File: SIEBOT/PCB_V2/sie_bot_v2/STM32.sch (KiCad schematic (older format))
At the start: 27 parts, among them P8 CONN_12X2, P9 CONN_12X2, U10 STM32F105RC, U11 LT1117CST-3.3, X3 8MHz

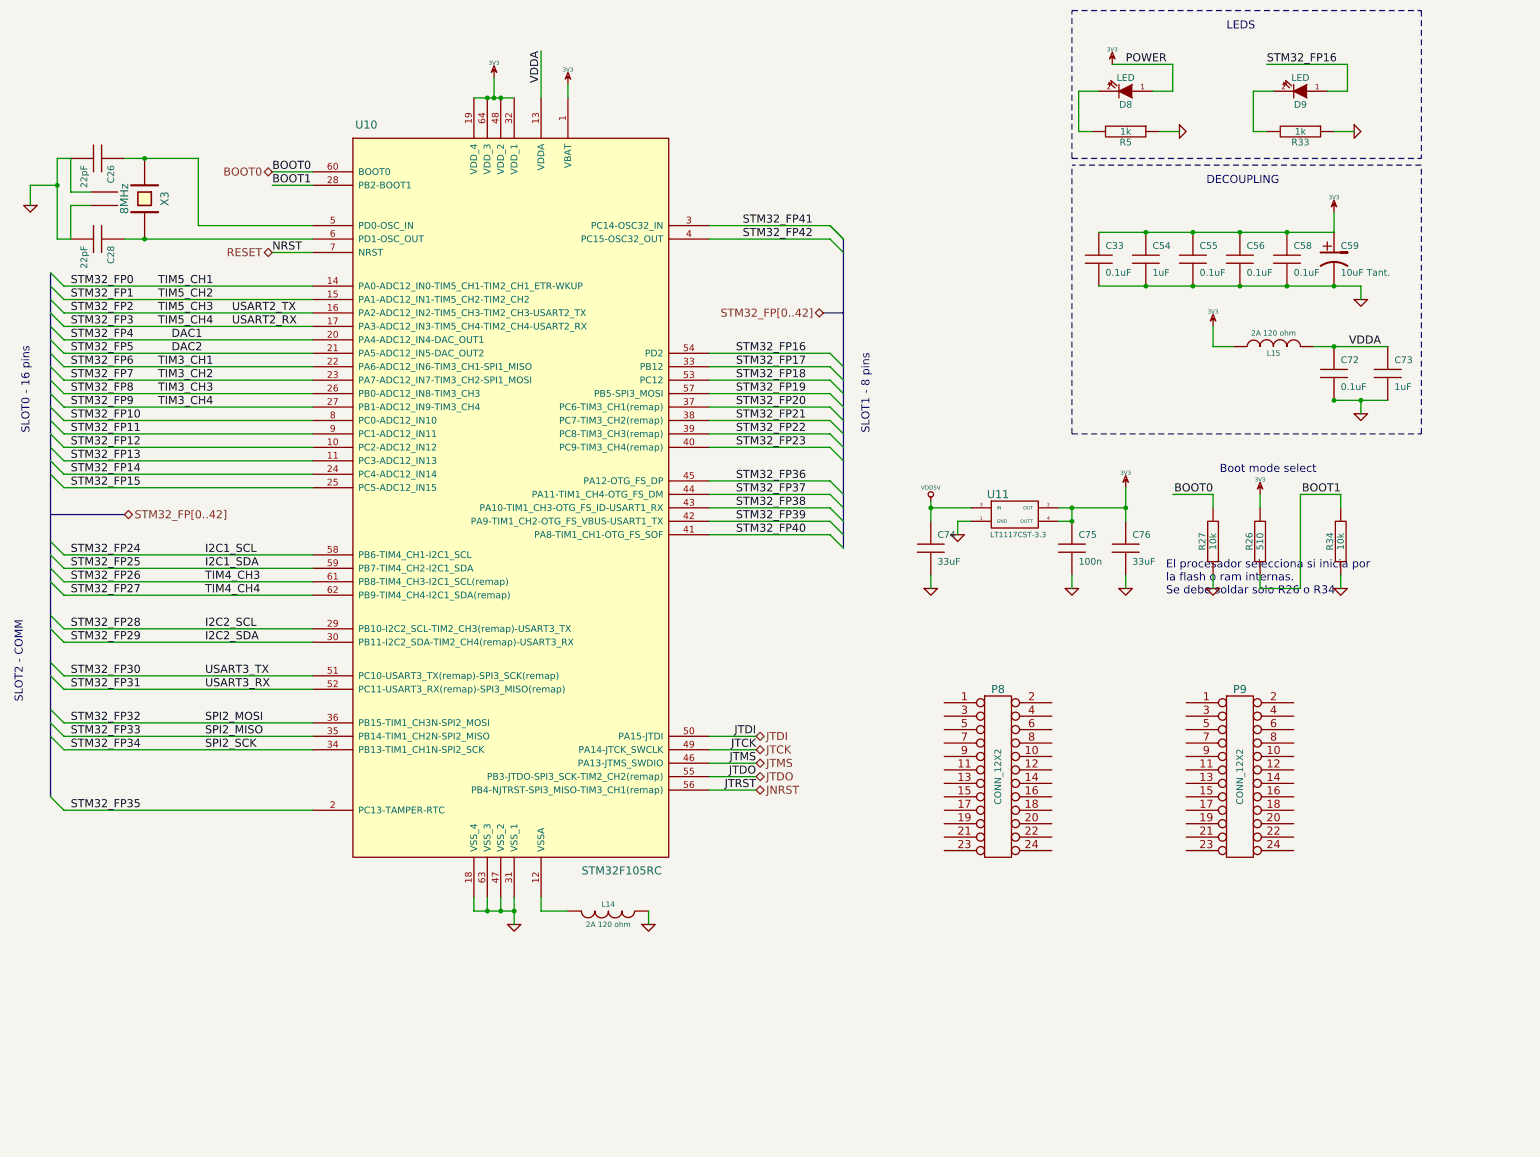
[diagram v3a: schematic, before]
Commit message: Coenxión y ruteo de los GPIO del STM32 t los conectores
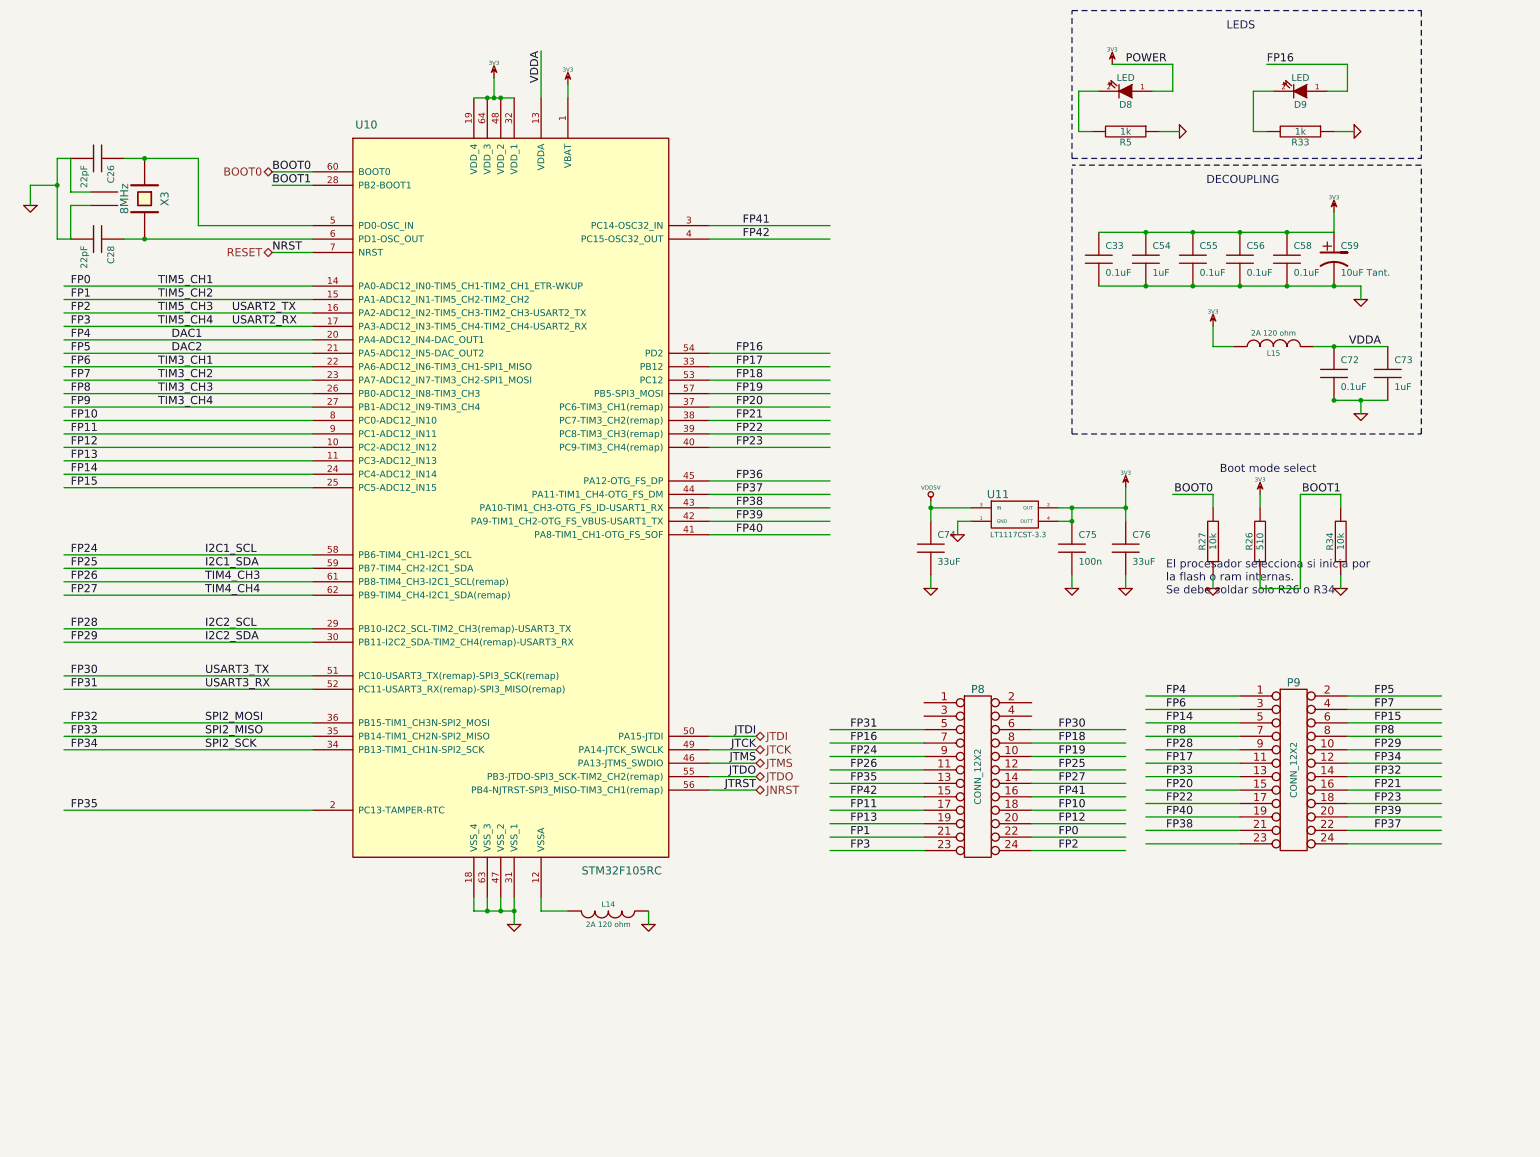
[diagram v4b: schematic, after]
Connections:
- net labels added: FP0, FP1, FP10, FP11, FP12, FP13, FP14, FP15, FP16, FP17, FP18, FP19, FP2, FP20, FP21, FP22, FP23, FP24, FP25, FP26, FP27, FP28, FP29, FP3, FP30, FP31, FP32, FP33, FP34, FP35, FP36, FP37, FP38, FP39, FP4, FP40, FP41, FP42, FP5, FP6, FP7, FP8, FP9
- net labels removed: STM32_FP0, STM32_FP1, STM32_FP10, STM32_FP11, STM32_FP12, STM32_FP13, STM32_FP14, STM32_FP15, STM32_FP16, STM32_FP17, STM32_FP18, STM32_FP19, STM32_FP2, STM32_FP20, STM32_FP21, STM32_FP22, STM32_FP23, STM32_FP24, STM32_FP25, STM32_FP26, STM32_FP27, STM32_FP28, STM32_FP29, STM32_FP3, STM32_FP30, STM32_FP31, STM32_FP32, STM32_FP33, STM32_FP34, STM32_FP35, STM32_FP36, STM32_FP37, STM32_FP38, STM32_FP39, STM32_FP4, STM32_FP40, STM32_FP41, STM32_FP42, STM32_FP5, STM32_FP6, STM32_FP7, STM32_FP8, STM32_FP9, STM32_FP[0..42]
- wire segments 120 -> 164
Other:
- note removed: "SLOT0 - 16 pins"
- note removed: "SLOT1 - 8 pins"
- note removed: "SLOT2 - COMM"
- moved on the sheet: P8, P9

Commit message: Adición de puentes H, finalización del ruteo de los pines del STM32
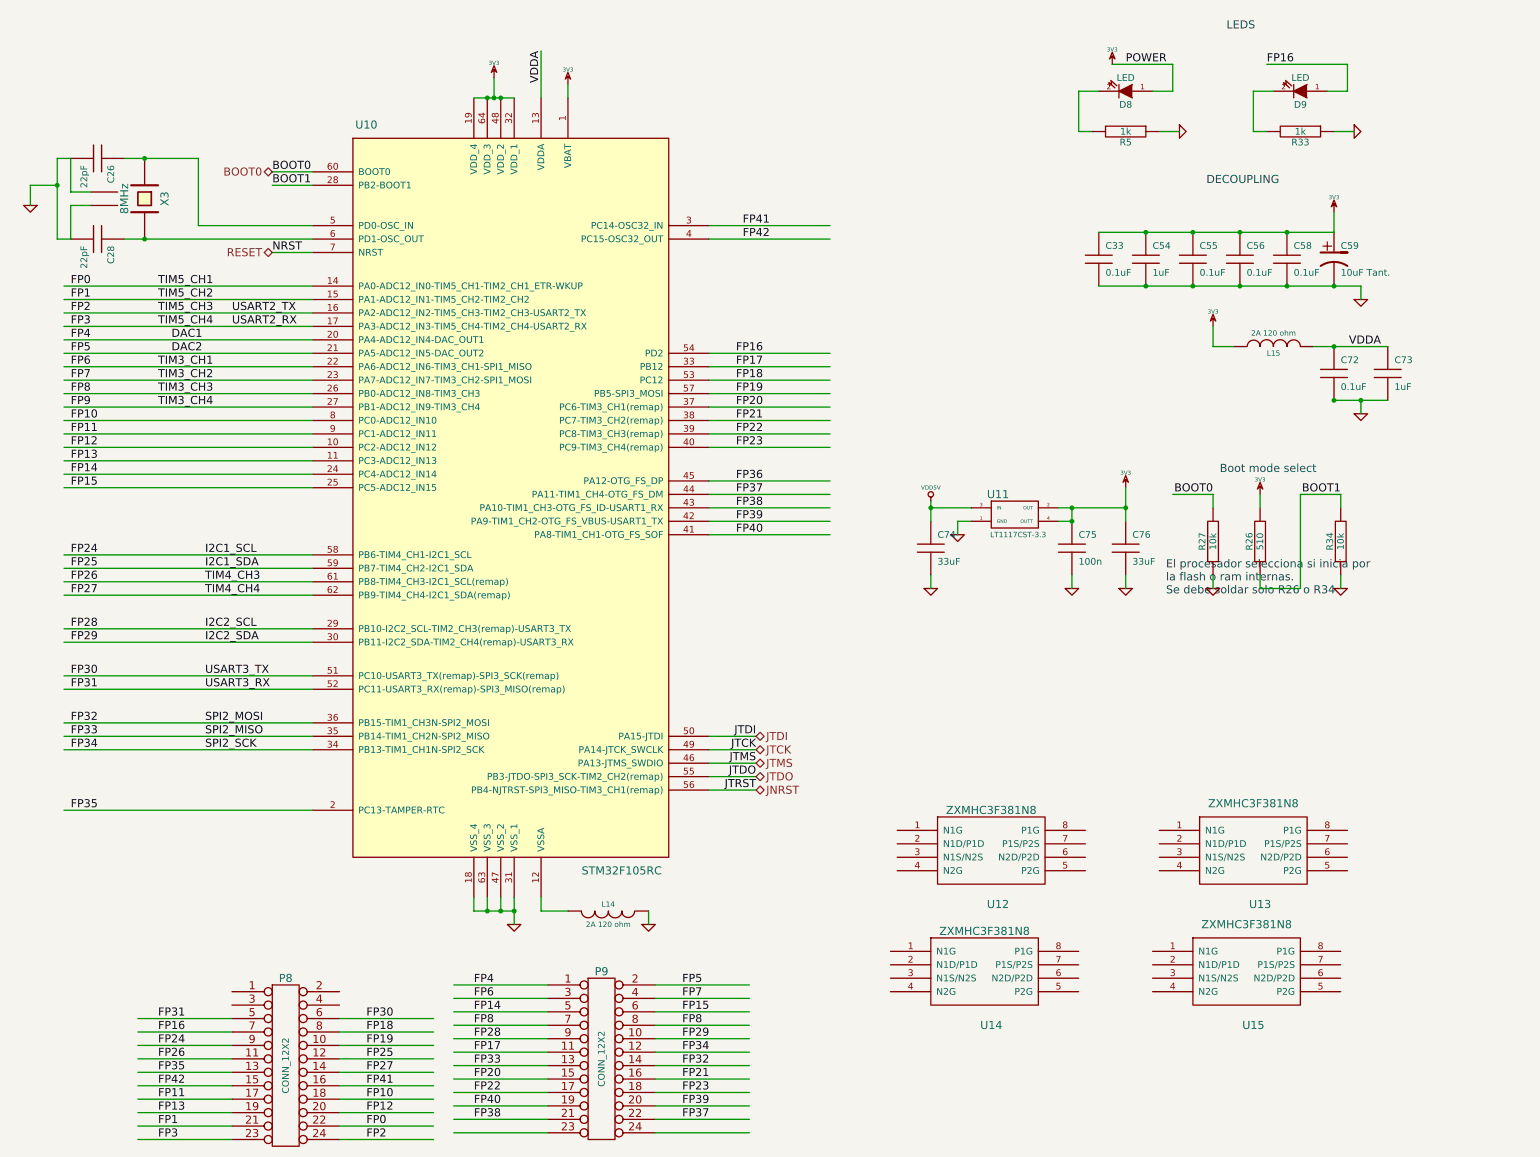
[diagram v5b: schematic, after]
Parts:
- added U12, U13, U14, U15: ZXMHC3F381N8, -SO8, symbol ZXMHC3F381N8
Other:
- moved on the sheet: P8, P9

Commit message: Inicio de la conexión de los Puente H
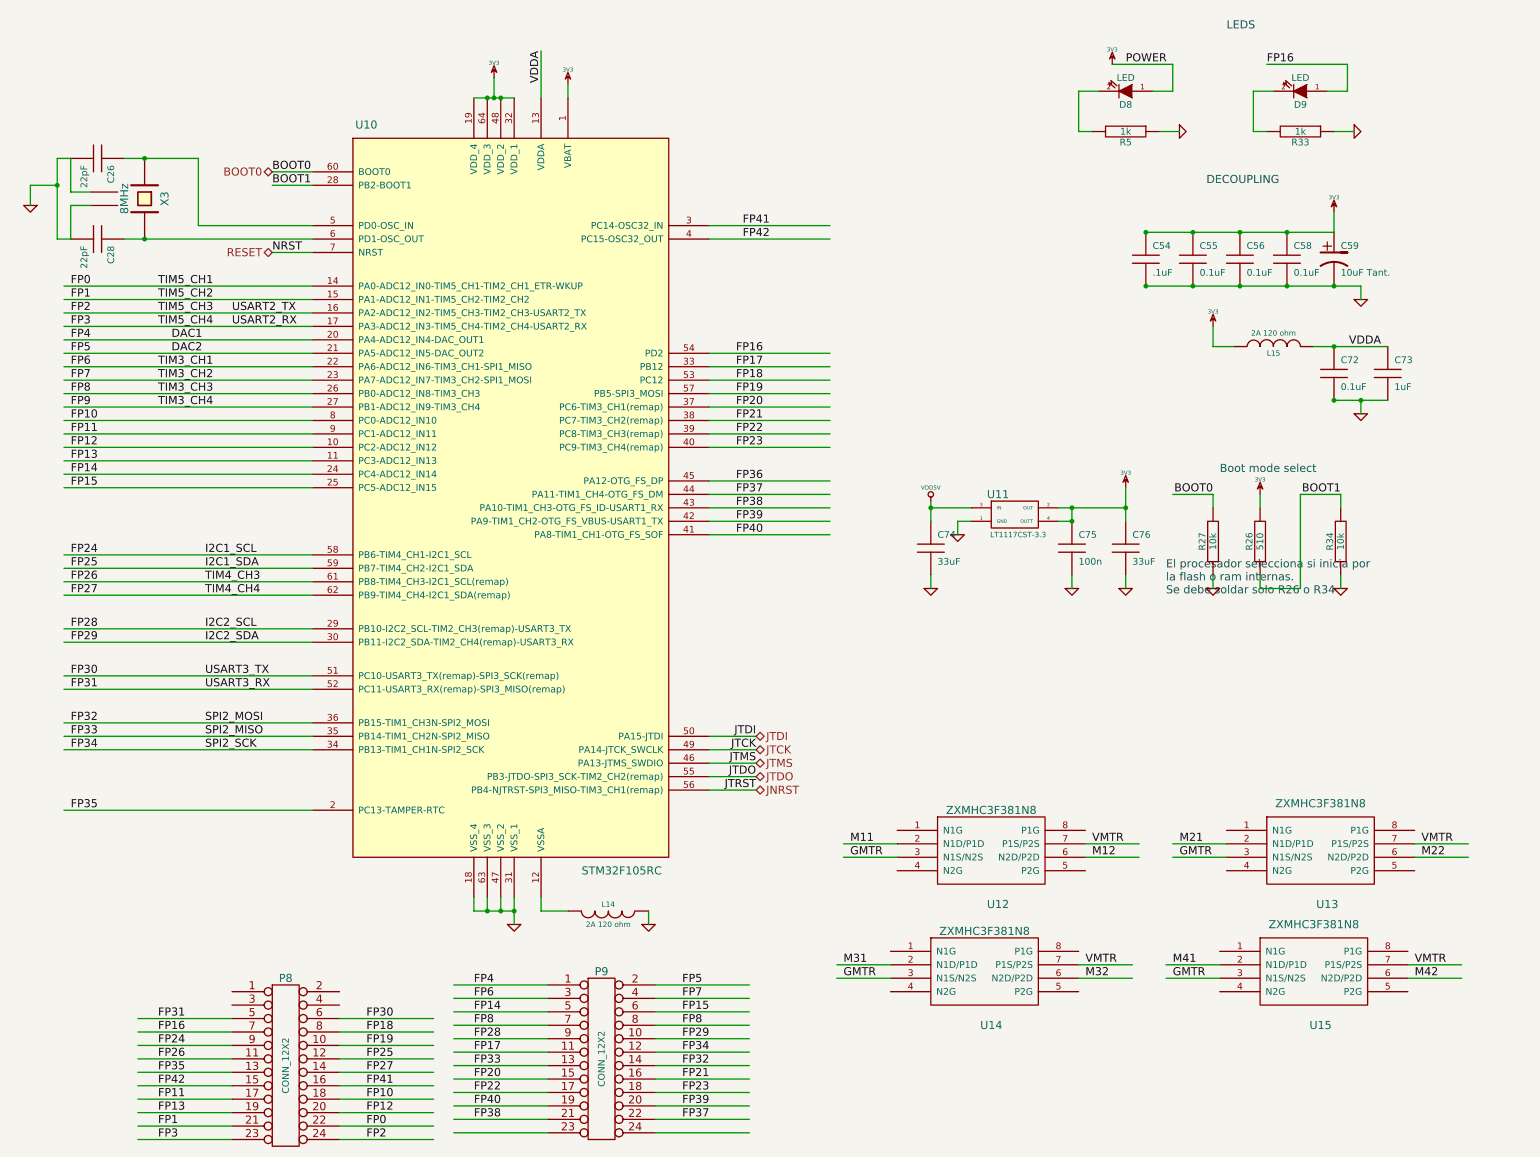
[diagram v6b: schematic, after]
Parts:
- removed C33: 0.1uF, SM0603, symbol C
- C54: value 1uF -> .1uF; footprint SM0805 -> SM0603
- X3: footprint ABM8G -> ABM3B
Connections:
- net labels added: GMTR, M11, M12, M21, M22, M31, M32, M41, M42, VMTR
- wire segments 164 -> 180
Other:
- moved on the sheet: U13, U15

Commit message: conexión del puente H, inicio de conexion con los conectores
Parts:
- added P11, P12, P13, P14: CONN_6, SIL-6, symbol CONN_6
- added Q2, Q3, Q4, Q5, Q6, Q7, Q8, Q9: BS170F, BS170F, symbol MOSFET_N_OPENDOUS
- added R35, R37, R38, R39, R40, R41, R42, R43: 2.2k, SM0603, symbol R
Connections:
- net labels added: C1M1, C1M2, C1M3, C1M4, C2M1, C2M2, C2M3, C2M4, GMTR1, GMTR2, GMTR3, GMTR4, VMTR1, VMTR2, VMTR3, VMTR4
- net labels removed: GMTR, VMTR
- wire segments 180 -> 236
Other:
- moved on the sheet: C54, C55, C56, C58, C59, C72, C73, C74, C75, C76, L15, R26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

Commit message: ruteo del primer puente H
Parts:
- removed P11, P12, P13, P14: CONN_6, SIL-6, symbol CONN_6
- added P11, P12, P13, P14: CONN_3X2, pin_array_3x2, symbol CONN_3X2
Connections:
- wire segments 236 -> 260
